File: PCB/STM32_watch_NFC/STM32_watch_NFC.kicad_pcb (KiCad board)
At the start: 4 copper layers, 40 x 40 mm, 122 parts, among them J1 Conn_01x06_Socket, J2 USB_C_Receptacle_PowerOnly_6P, Q1 2N7000, SW1 SW_DPST_x2, SW2 SW_DPST_x2, SW3 SW_DPST_x2, U1 STM32L031G6Ux, U2 MIC5365-3.3YC5, U3 ST25R3916-AQWT, U4 MT3608, Y1 27.12Mhz, Y2 32.768kHz

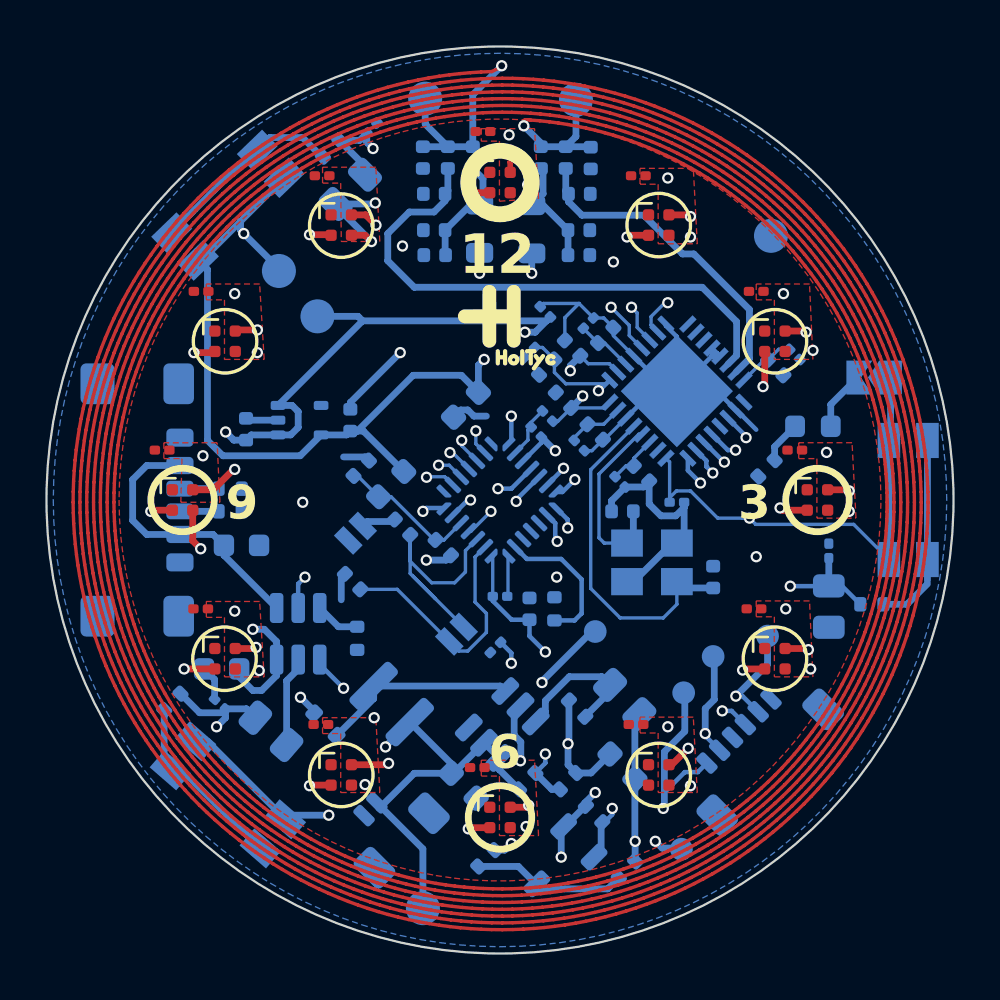
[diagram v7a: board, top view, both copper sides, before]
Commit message: Kicad - new Routing 2
4 7-segment RGB displays for time - pretty crazy I would say
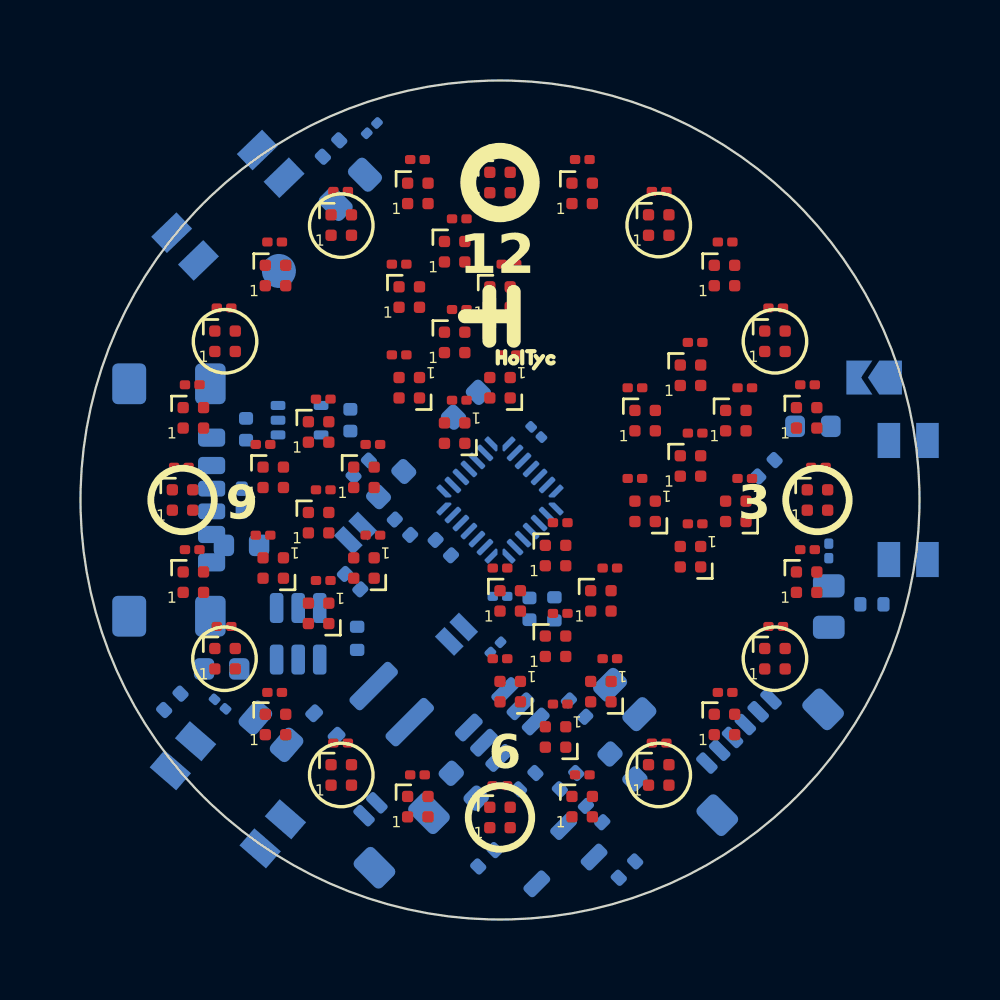
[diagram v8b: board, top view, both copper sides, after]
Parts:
- removed +BAT: 2.7-4.2V, TestPoint:TestPoint_Pad_D1.5mm
- removed 5V: 5V, TestPoint:TestPoint_Pad_D1.5mm
- removed A1, A2: ~, TestPoint:TestPoint_Pad_D1.5mm
- removed CLK, DINS, DIO, D_BAT, NRST: ~, TestPoint:TestPoint_Pad_D1.0mm
- removed GND: GND, TestPoint:TestPoint_Pad_D1.5mm
- removed L2, L3: 270nH 500mOhm, Inductor_SMD:L_0805_2012Metric
- removed U3: ST25R3916-AQWT, ST25R3916-AQWT:QFN50P500X500X100-33N
- removed Y1: 27.12Mhz, Crystal:Crystal_SMD_3225-4Pin_3.2x2.5mm
- added C32: 100n, Capacitor_SMD:C_0201_0603Metric, F.Cu at (144.9, 90.0)
- added C33: 100n, Capacitor_SMD:C_0201_0603Metric, F.Cu at (141.5, 91.4)
- added C62: 100n, Capacitor_SMD:C_0201_0603Metric, F.Cu at (138.1, 102.5)
- added C63: 100n, Capacitor_SMD:C_0201_0603Metric, F.Cu at (140.7, 100.5)
- added C64: 100n, Capacitor_SMD:C_0201_0603Metric, F.Cu at (146.7, 100.6)
- added C65: 100n, Capacitor_SMD:C_0201_0603Metric, F.Cu at (148.9, 98.6)
- added C66: 100n, Capacitor_SMD:C_0201_0603Metric, F.Cu at (144.1, 98.6)
- added C67: 100n, Capacitor_SMD:C_0201_0603Metric, F.Cu at (146.7, 96.6)
- added C68: 100n, Capacitor_SMD:C_0201_0603Metric, F.Cu at (148.9, 94.6)
- added C69: 100n, Capacitor_SMD:C_0201_0603Metric, F.Cu at (144.1, 94.6)
- added C70: 100n, Capacitor_SMD:C_0201_0603Metric, F.Cu at (146.7, 92.6)
- added D15: SK6805, LED_SMD:LED_SK6812_EC15_1.5x1.5mm, F.Cu at (148.5, 91.0)
- added D16: SK6805, LED_SMD:LED_SK6812_EC15_1.5x1.5mm, F.Cu at (144.9, 91.5)
- added D17: SK6805, LED_SMD:LED_SK6812_EC15_1.5x1.5mm, F.Cu at (141.5, 92.9)
- added D18: SK6805, LED_SMD:LED_SK6812_EC15_1.5x1.5mm, F.Cu at (138.6, 95.1)
- added D19: SK6805, LED_SMD:LED_SK6812_EC15_1.5x1.5mm, F.Cu at (136.4, 98.0)
- added D20: SK6805, LED_SMD:LED_SK6812_EC15_1.5x1.5mm, F.Cu at (135.0, 101.4)
- added D21: SK6805, LED_SMD:LED_SK6812_EC15_1.5x1.5mm, F.Cu at (134.5, 105.0)
- added D22: SK6805, LED_SMD:LED_SK6812_EC15_1.5x1.5mm, F.Cu at (135.0, 108.6)
- added D23: SK6805, LED_SMD:LED_SK6812_EC15_1.5x1.5mm, F.Cu at (136.4, 112.0)
- added D24: SK6805, LED_SMD:LED_SK6812_EC15_1.5x1.5mm, F.Cu at (138.6, 114.9)
- added D25: SK6805, LED_SMD:LED_SK6812_EC15_1.5x1.5mm, F.Cu at (141.5, 117.1)
- added D26: SK6805, LED_SMD:LED_SK6812_EC15_1.5x1.5mm, F.Cu at (144.9, 118.5)
- added D27: SK6805, LED_SMD:LED_SK6812_EC15_1.5x1.5mm, F.Cu at (150.9, 115.5)
- added D28: SK6805, LED_SMD:LED_SK6812_EC15_1.5x1.5mm, F.Cu at (152.9, 113.5)
- added D29: SK6805, LED_SMD:LED_SK6812_EC15_1.5x1.5mm, F.Cu at (148.9, 113.5)
- added D30: SK6805, LED_SMD:LED_SK6812_EC15_1.5x1.5mm, F.Cu at (150.9, 111.5)
- added D31: SK6805, LED_SMD:LED_SK6812_EC15_1.5x1.5mm, F.Cu at (152.9, 109.5)
- added D32: SK6805, LED_SMD:LED_SK6812_EC15_1.5x1.5mm, F.Cu at (148.9, 109.5)
- added D33: SK6805, LED_SMD:LED_SK6812_EC15_1.5x1.5mm, F.Cu at (150.9, 107.5)
- added D34: SK6805, LED_SMD:LED_SK6812_EC15_1.5x1.5mm, F.Cu at (156.9, 107.5)
- added D35: SK6805, LED_SMD:LED_SK6812_EC15_1.5x1.5mm, F.Cu at (158.9, 105.5)
- added D36: SK6805, LED_SMD:LED_SK6812_EC15_1.5x1.5mm, F.Cu at (154.9, 105.5)
- added D37: SK6805, LED_SMD:LED_SK6812_EC15_1.5x1.5mm, F.Cu at (156.9, 103.5)
- added D38: SK6805, LED_SMD:LED_SK6812_EC15_1.5x1.5mm, F.Cu at (158.9, 101.5)
- added D39: SK6805, LED_SMD:LED_SK6812_EC15_1.5x1.5mm, F.Cu at (154.9, 101.5)
- added D40: SK6805, LED_SMD:LED_SK6812_EC15_1.5x1.5mm, F.Cu at (156.9, 99.5)
- added D41: SK6805, LED_SMD:LED_SK6812_EC15_1.5x1.5mm, F.Cu at (140.5, 110.0)
- added D42: SK6805, LED_SMD:LED_SK6812_EC15_1.5x1.5mm, F.Cu at (142.5, 108.0)
- added D43: SK6805, LED_SMD:LED_SK6812_EC15_1.5x1.5mm, F.Cu at (138.5, 108.0)
- added D44: SK6805, LED_SMD:LED_SK6812_EC15_1.5x1.5mm, F.Cu at (140.5, 106.0)
- added D45: SK6805, LED_SMD:LED_SK6812_EC15_1.5x1.5mm, F.Cu at (142.5, 104.0)
- added D46: SK6805, LED_SMD:LED_SK6812_EC15_1.5x1.5mm, F.Cu at (138.5, 104.0)
- added D47: SK6805, LED_SMD:LED_SK6812_EC15_1.5x1.5mm, F.Cu at (140.5, 102.0)
- added D48: SK6805, LED_SMD:LED_SK6812_EC15_1.5x1.5mm, F.Cu at (146.5, 102.0)
- added D49: SK6805, LED_SMD:LED_SK6812_EC15_1.5x1.5mm, F.Cu at (148.5, 100.0)
- added D50: SK6805, LED_SMD:LED_SK6812_EC15_1.5x1.5mm, F.Cu at (144.5, 100.0)
- added D51: SK6805, LED_SMD:LED_SK6812_EC15_1.5x1.5mm, F.Cu at (146.5, 98.0)
- added D52: SK6805, LED_SMD:LED_SK6812_EC15_1.5x1.5mm, F.Cu at (148.5, 96.0)
- added D53: SK6805, LED_SMD:LED_SK6812_EC15_1.5x1.5mm, F.Cu at (144.5, 96.0)
- added D54: SK6805, LED_SMD:LED_SK6812_EC15_1.5x1.5mm, F.Cu at (146.5, 94.0)
- C31: moved to F.Cu
- C34, C36, C38, C40, C42, C44, C47: value 22n -> 100n; moved to F.Cu
- C35, C37, C39, C41, C43, C45: value 2.2uF -> 100n; footprint Capacitor_SMD:C_0402_1005Metric -> Capacitor_SMD:C_0201_0603Metric; moved to F.Cu
- C46: value 1u -> 100n; footprint Capacitor_SMD:C_0402_1005Metric -> Capacitor_SMD:C_0201_0603Metric; moved to F.Cu
- C48, C49, C50, C51, C58, C59: value 15pF -> 100n; footprint Capacitor_SMD:C_0402_1005Metric -> Capacitor_SMD:C_0201_0603Metric; moved to F.Cu
- C52, C53, C54, C55, C57, C61: value 220pF -> 100n; footprint Capacitor_SMD:C_0402_1005Metric -> Capacitor_SMD:C_0201_0603Metric; moved to F.Cu
- C56, C60: value 10pF -> 100n; footprint Capacitor_SMD:C_0402_1005Metric -> Capacitor_SMD:C_0201_0603Metric; moved to F.Cu
- moved C12 28.9 mm to (148.5, 117.6), turned to 180 degrees
- moved C20 28.6 mm to (160.7, 96.5), turned to 180 degrees
- moved D9 28.0 mm to (160.6, 98.0)
- moved D1 28.0 mm to (148.5, 119.0)
- moved C13 26.5 mm to (152.1, 117.1), turned to 180 degrees
- moved C21 26.5 mm to (158.4, 93.6), turned to 180 degrees
- moved C19 26.2 mm to (162.1, 99.9), turned to 180 degrees
- moved D8 25.9 mm to (162.0, 101.4)
- moved D2 25.9 mm to (152.1, 118.5)
- moved D10 25.9 mm to (158.4, 95.1)
- moved C59 22.0 mm to (138.1, 106.5), turned to 0 degrees
- moved C42 21.2 mm to (144.9, 117.1), turned to 180 degrees
- moved C39 21.2 mm to (136.3, 110.6), turned to 180 degrees
- moved C22 20.7 mm to (155.5, 91.4), turned to 180 degrees
- moved C14 20.4 mm to (155.5, 115.7), turned to 180 degrees
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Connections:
- C31 pad 1: +3.3V -> +5V
- C34 pad 1: Net-(U3-VDD_D) -> +5V
- C35 pad 1: GND -> +5V
- C35 pad 2: Net-(U3-VDD_D) -> GND
- C36 pad 1: Net-(U3-VDD_A) -> +5V
- C37 pad 1: GND -> +5V
- C37 pad 2: Net-(U3-VDD_A) -> GND
- C38 pad 1: Net-(U3-VDD_AM) -> +5V
- C39 pad 1: GND -> +5V
- C39 pad 2: Net-(U3-VDD_AM) -> GND
- C40 pad 1: Net-(U3-VDD_DR) -> +5V
- C41 pad 1: GND -> +5V
- C41 pad 2: Net-(U3-VDD_DR) -> GND
- C43 pad 1: GND -> +5V
- C43 pad 2: +5V -> GND
- C45 pad 1: GND -> +5V
- C45 pad 2: +5V -> GND
- C46 pad 1: GND -> +5V
- C46 pad 2: Net-(U3-AGDC) -> GND
- C47 pad 1: Net-(U3-AGDC) -> +5V
- C48 pad 1: GND -> +5V
- C48 pad 2: Net-(U3-XTI) -> GND
- C49 pad 1: GND -> +5V
- C49 pad 2: Net-(U3-XTO) -> GND
- C50 pad 1: Net-(C50-Pad1) -> +5V
- C50 pad 2: /NFC_RFID/A2 -> GND
- C51 pad 1: Net-(C51-Pad1) -> +5V
- C51 pad 2: /NFC_RFID/A1 -> GND
- C52 pad 1: Net-(C50-Pad1) -> +5V
- C53 pad 1: GND -> +5V
- C53 pad 2: Net-(C51-Pad1) -> GND
- C54 pad 1: GND -> +5V
- C54 pad 2: Net-(C50-Pad1) -> GND
- C55 pad 1: Net-(C51-Pad1) -> +5V
- C56 pad 1: Net-(U3-RFI1) -> +5V
- C56 pad 2: /NFC_RFID/A1 -> GND
- C57 pad 1: GND -> +5V
- C57 pad 2: Net-(U3-RFI1) -> GND
- C58 pad 1: GND -> +5V
- C58 pad 2: /NFC_RFID/A1 -> GND
- C59 pad 1: /NFC_RFID/A2 -> +5V
- C60 pad 1: Net-(U3-RFI2) -> +5V
- C60 pad 2: /NFC_RFID/A2 -> GND
- C61 pad 1: GND -> +5V
- C61 pad 2: Net-(U3-RFI2) -> GND
- D12 pad 1: Net-(D1-DIN) -> Net-(D12-DOUT)
- D6 pad 1: unconnected-(D6-DOUT-Pad1) -> Net-(D6-DOUT)
- D7 pad 3: Net-(D7-DIN) -> Net-(D6-DOUT)
- R6 pad 1: DIN_LED -> DIN_STM
- R6 pad 2: Net-(D7-DIN) -> Net-(D1-DIN)
- U1 pad 10: SPI_CS_STM -> unconnected-(U1-PA4-Pad10)
- U1 pad 11: SPI_SCL_STM -> unconnected-(U1-PA5-Pad11)
- U1 pad 12: SPI_MISO_STM -> unconnected-(U1-PA6-Pad12)
- U1 pad 13: SPI_MOSI_STM -> unconnected-(U1-PA7-Pad13)
- U1 pad 9: SPI_IRQ_STM -> unconnected-(U1-PA3-Pad9)
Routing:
- net /NFC_RFID/A1: track 797.8 -> 0.00 mm, vias 1 -> 0
- net GND: track 236.3 -> 0.00 mm, vias 32 -> 0
- net +3.3V: track 152.2 -> 0.00 mm, vias 8 -> 0
- net +5V: track 76.9 -> 0.00 mm, vias 6 -> 0
- net /NRST: track 33.8 -> 0.00 mm, vias 3 -> 0
- net +BATT: track 32.1 -> 0.00 mm, vias 2 -> 0
- net /SWCLK: track 24.5 -> 0.00 mm, vias 2 -> 0
- net Net-(U3-RFI1): track 24.3 -> 0.00 mm
- net Button_LT: track 24.3 -> 0.00 mm, vias 2 -> 0
- net DIN_STM: track 23.0 -> 0.00 mm, vias 4 -> 0
- net BATT_STM: track 22.4 -> 0.00 mm, vias 3 -> 0
- net Button_LB: track 21.9 -> 0.00 mm, vias 2 -> 0
- net /SWDIO: track 21.5 -> 0.00 mm, vias 2 -> 0
- net SPI_IRQ_STM: track 20.2 -> 0.00 mm, vias 2 -> 0
- net SPI_CS_STM: track 19.5 -> 0.00 mm, vias 2 -> 0
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- removed copper zone on F.Cu, net +5V
- removed copper zone on B.Cu, net GND
- removed copper zone on F.Cu, net GND
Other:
- board size 40 x 40 mm -> 37 x 37 mm
- board text added: "Rev.B.0"
- board text removed: "Rev.A.0"
